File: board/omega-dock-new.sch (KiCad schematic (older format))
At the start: 16 parts, among them J1 USB_A, J2 USB_PWR, J3 RJ45-TRANSFO, U1 USBLC6-2, U2 AP111733

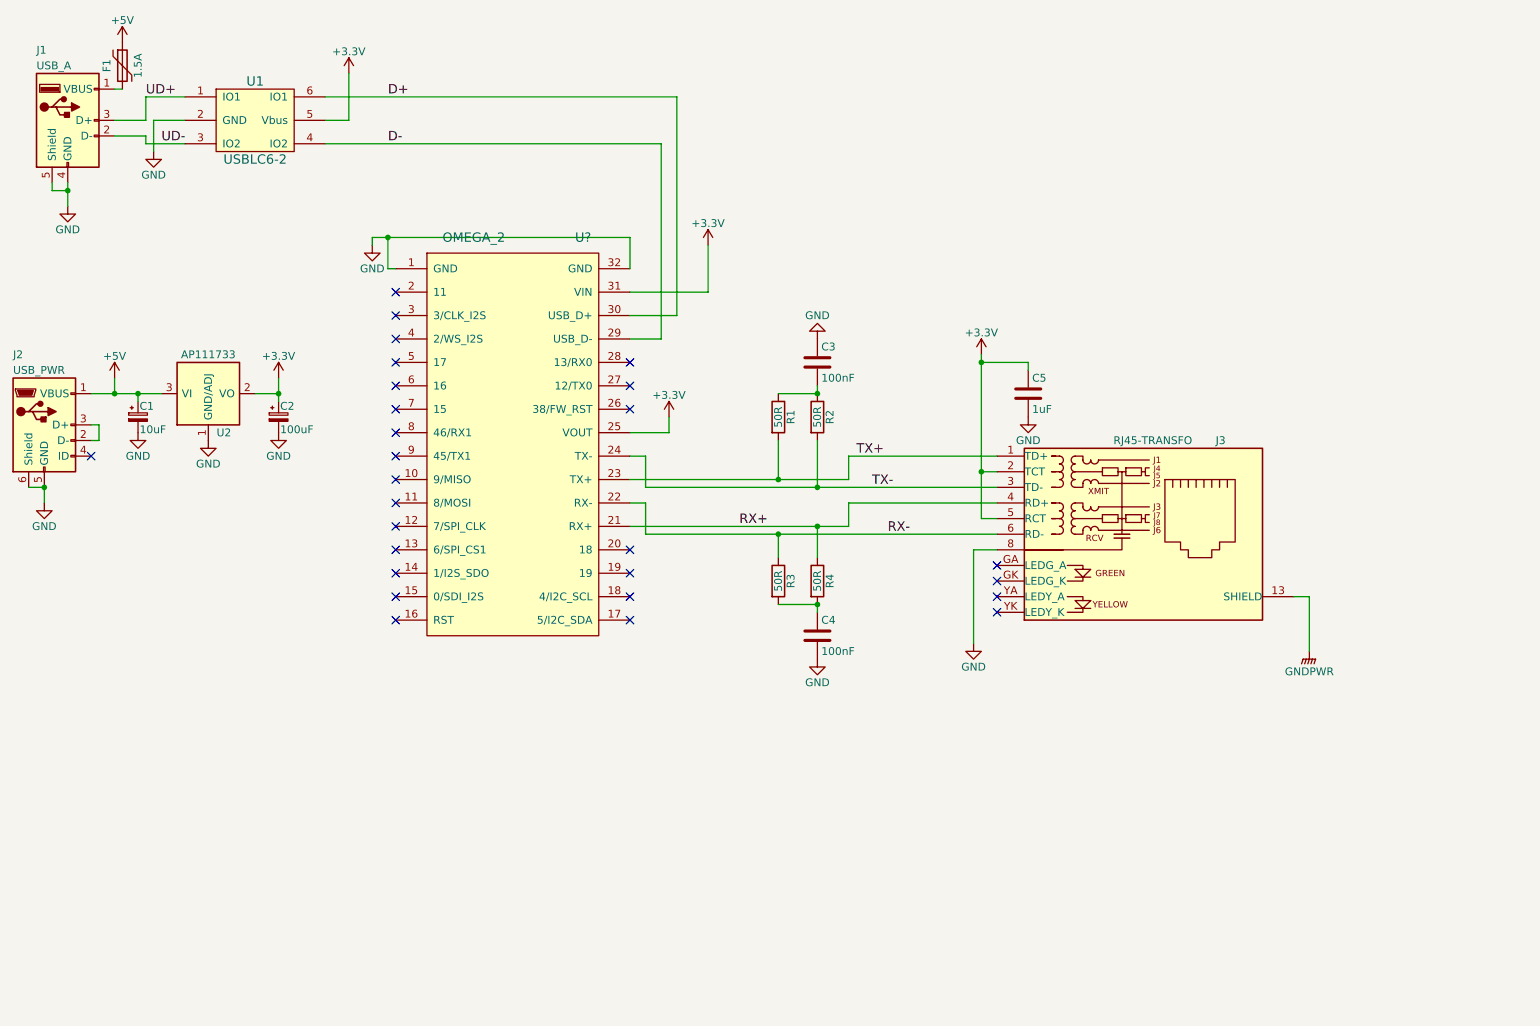
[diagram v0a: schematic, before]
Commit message: v1.0 fixes #1, fixes #2, fixes #3, fixes #4, fixes #5, fixes #7, fixes #8
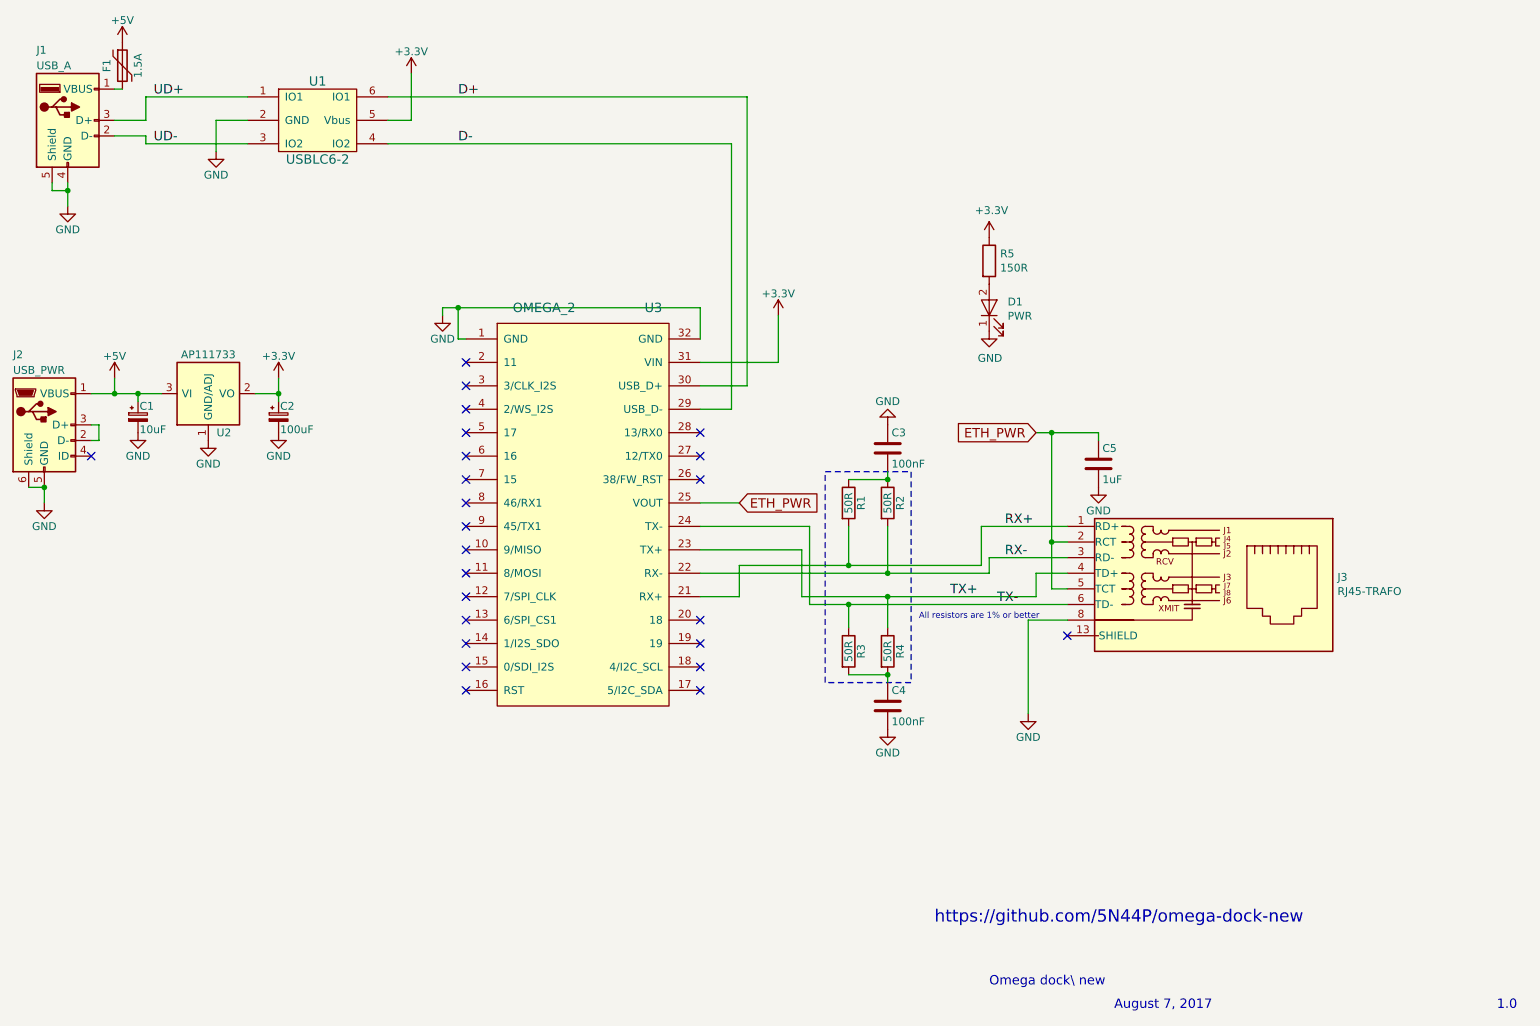
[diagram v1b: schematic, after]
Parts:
- removed J3: RJ45-TRANSFO, symbol RJ45-TRANSFO
- added D1: PWR, LEDs:LED_1206_HandSoldering, symbol LED
- added J3: RJ45-TRAFO, RJ45-TRAFO-AMPHENOL:RJ45_TRAFO_AMPHENOL, symbol RJ45-TRAFO
- added R5: 150R, Resistors_SMD:R_0805_HandSoldering, symbol R
- R1, R2, R3, R4: footprint Resistors_SMD:R_0805 -> Resistors_SMD:R_0805_HandSoldering
- gave numbers to parts that had none: 1
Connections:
- net +3V3: now also R5.1; no longer C5.1, U3.25 (VOUT)
- net GND: now also D1.1 (K), J3.8
- net RX+: now also R1.2, J3.1 (RD+); no longer R4.1
- net RX-: now also R2.2, J3.3 (RD-); no longer R3.1
- net TX+: now also R4.1, J3.4 (TD+); no longer R1.2
- net TX-: now also R3.1, J3.6 (TD-); no longer R2.2
- new net: D1.2 (A), R5.2
- new net ETH_PWR: C5.1, J3.2 (RCT), J3.5 (TCT), U3.25 (VOUT)
- no-connect marks 27 -> 24
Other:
- note added: "1.0"
- note added: "All resistors are 1% or better"
- note added: "August 7, 2017"
- note added: "Omega dock\ new"
- note added: "https://github.com/5N44P/omega-dock-new"
- moved on the sheet: C3, C4, C5, R1, R2, R3, R4, U1, U3
